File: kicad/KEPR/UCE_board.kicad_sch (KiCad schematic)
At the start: 10 parts, among them U2 STM32G484CETx

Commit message: Mais ajustes no roteamento
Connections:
- net +3.3V: now also U2.9 (PA1)
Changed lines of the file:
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@@
+	(wire
+		(pts
+			(xy 231.14 116.84) (xy 236.22 116.84)
+		)
+		(stroke
+			(width 0)
+			(type default)
+		)
+	)
 	(wire
 		(pts

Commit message: Ajustes no Power Rail, entre outros ajustes.
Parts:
- R2: value GMR320HJAAFD5L00 -> GMR320HJAAFM5L00
- R3: value GMR320HJAAFD5L00 -> GMR320HJAAFS5L00
- R4: value GMR320HJAAFD5L00 -> GMR320HJAAFE5L00
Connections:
- net +3.3V: no longer U2.9 (PA1)
- net I2C_SDA_MCU_CTL: now reaches U2.37 (PA13)
- net I2C_SCL_MCU_CTL: now reaches U2.38 (PA14)
- new net +3.3v Shunt Out: U2.9 (PA1)

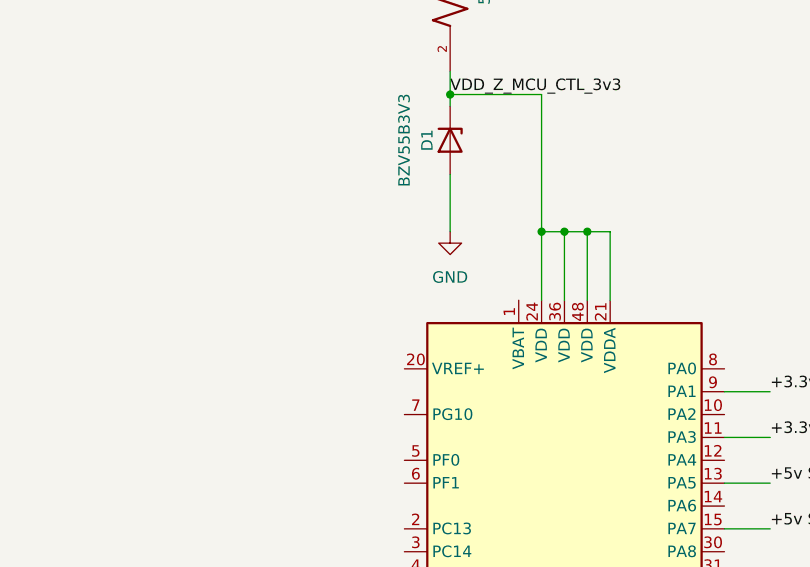
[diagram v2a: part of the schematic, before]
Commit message: Adicionado holder para bateria.
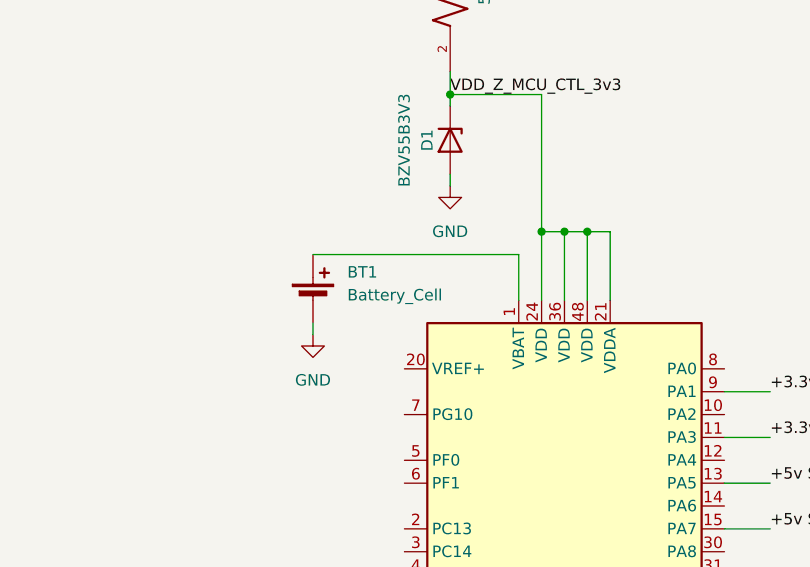
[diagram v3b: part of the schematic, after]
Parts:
- added BT1: Battery_Cell, Battery:BatteryHolder_Multicomp_BC-2001_1x2032, symbol Device:Battery_Cell
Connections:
- net GND: now also BT1.2 (-)
- net at U2.1 (VBAT): now also BT1.1 (+)
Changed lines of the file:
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@@
 	(wire
 		(pts
-			(xy 200.66 92.71) (xy 200.66 99.06)
+			(xy 200.66 92.71) (xy 200.66 93.98)
 		)
 		(stroke
@@
 	(wire
 		(pts
+			(xy 208.28 101.6) (xy 208.28 106.68)
+		)
+		(stroke
+			(width 0)
+			(type default)
+		)
+	)
+	(wire
+		(pts
 			(xy 147.32 236.22) (xy 147.32 246.38)
 		)
@@
 		(pts
 			(xy 200.66 83.82) (xy 200.66 85.09)
+		)
+		(stroke
+			(width 0)
+			(type default)
+		)
+	)
+	(wire
+		(pts
+			(xy 185.42 101.6) (xy 208.28 101.6)
+		)
+		(stroke
+			(width 0)
+			(type default)
+		)
+	)
+	(wire
+		(pts
+			(xy 185.42 109.22) (xy 185.42 110.49)
 		)
 		(stroke
@@
 	(symbol
 		(lib_id "power:GND")
+		(at 185.42 110.49 0)
+		(unit 1)
+		(exclude_from_sim no)
+		(in_bom yes)
+		(on_board yes)
+		(dnp no)
+		(fields_autoplaced yes)
+		(property "Reference" "#PWR02"
+			(at 185.42 116.84 0)
+			(effects
+				(font
+					(size 1.27 1.27)
+				)
+				(hide yes)
+			)
+		)
+		(property "Value" "GND"
+			(at 185.42 115.57 0)
+			(effects
+				(font
+					(size 1.27 1.27)
+				)
+			)
+		)
+		(property "Footprint" ""
+			(at 185.42 110.49 0)
+			(effects
+				(font
+					(size 1.27 1.27)
+				)
+				(hide yes)
+			)
+		)
+		(property "Datasheet" ""
+			(at 185.42 110.49 0)
+			(effects
+				(font
+					(size 1.27 1.27)
+				)
+				(hide yes)
+			)
+		)
+		(property "Description" "Power symbol creates a global label with name \"GND\" , ground"
+			(at 185.42 110.49 0)
+			(effects
+				(font
+					(size 1.27 1.27)
+				)
+				(hide yes)
+			)
+		)
+		(pin "1"
+		)
+		(instances
+			(project "KEPR"
+				(path "/5d9e1dfb-5ec5-4e06-bbdb-9cbfa1c0b9f1/fdc41c7f-76d0-4a6a-9947-620e5325b70e"
+					(reference "#PWR02")
+					(unit 1)
+				)
+			)
+		)
+	)
+	(symbol
+		(lib_id "Device:Battery_Cell")
+		(at 185.42 106.68 0)
+		(unit 1)
+		(exclude_from_sim no)
+		(in_bom yes)
+		(on_board yes)
+		(dnp no)
+		(fields_autoplaced yes)
+		(property "Reference" "BT1"
+			(at 189.23 103.5684 0)
+			(effects
+				(font
+					(size 1.27 1.27)
+				)
+				(justify left)
+			)
+		)
+		(property "Value" "Battery_Cell"
+			(at 189.23 106.1084 0)
+			(effects
+				(font
+					(size 1.27 1.27)
+				)
+				(justify left)
+			)
+		)
+		(property "Footprint" "Battery:BatteryHolder_Multicomp_BC-2001_1x2032"
+			(at 185.42 105.156 90)
+			(effects
+				(font
+					(size 1.27 1.27)
+				)
+				(hide yes)
+			)
+		)
+		(property "Datasheet" "~"
+			(at 185.42 105.156 90)
+			(effects
+				(font
+					(size 1.27 1.27)
+				)
+				(hide yes)
+			)
+		)
+		(property "Description" "Single-cell battery"
+			(at 185.42 106.68 0)
+			(effects
+				(font
+					(size 1.27 1.27)
+				)
+				(hide yes)
+			)
+		)
+		(pin "1"
+		)
+		(pin "2"
+		)
+		(instances
+			(project ""
+				(path "/5d9e1dfb-5ec5-4e06-bbdb-9cbfa1c0b9f1/fdc41c7f-76d0-4a6a-9947-620e5325b70e"
+					(reference "BT1")
+					(unit 1)
+				)
+			)
+		)
+	)
+	(symbol
+		(lib_id "power:GND")
 		(at 147.32 259.08 0)
 		(unit 1)
@@
 	(symbol
 		(lib_id "power:GND")
-		(at 200.66 99.06 0)
+		(at 200.66 93.98 0)
 		(unit 1)
 		(exclude_from_sim no)
@@
 		(fields_autoplaced yes)
 		(property "Reference" "#PWR034"
-			(at 200.66 105.41 0)
+			(at 200.66 100.33 0)
 			(effects
 				(font
@@
 		)
 		(property "Value" "GND"
-			(at 200.66 104.14 0)
+			(at 200.66 99.06 0)
 			(effects
 				(font
@@
 		)
 		(property "Footprint" ""
-			(at 200.66 99.06 0)
+			(at 200.66 93.98 0)
 			(effects
 				(font
@@
 		)
 		(property "Datasheet" ""
-			(at 200.66 99.06 0)
+			(at 200.66 93.98 0)
 			(effects
 				(font
@@
 		)
 		(property "Description" "Power symbol creates a global label with name \"GND\" , ground"
-			(at 200.66 99.06 0)
-			(effects
-				(font
+			(at 200.66 93.98 0)
+			(effects
+				(font

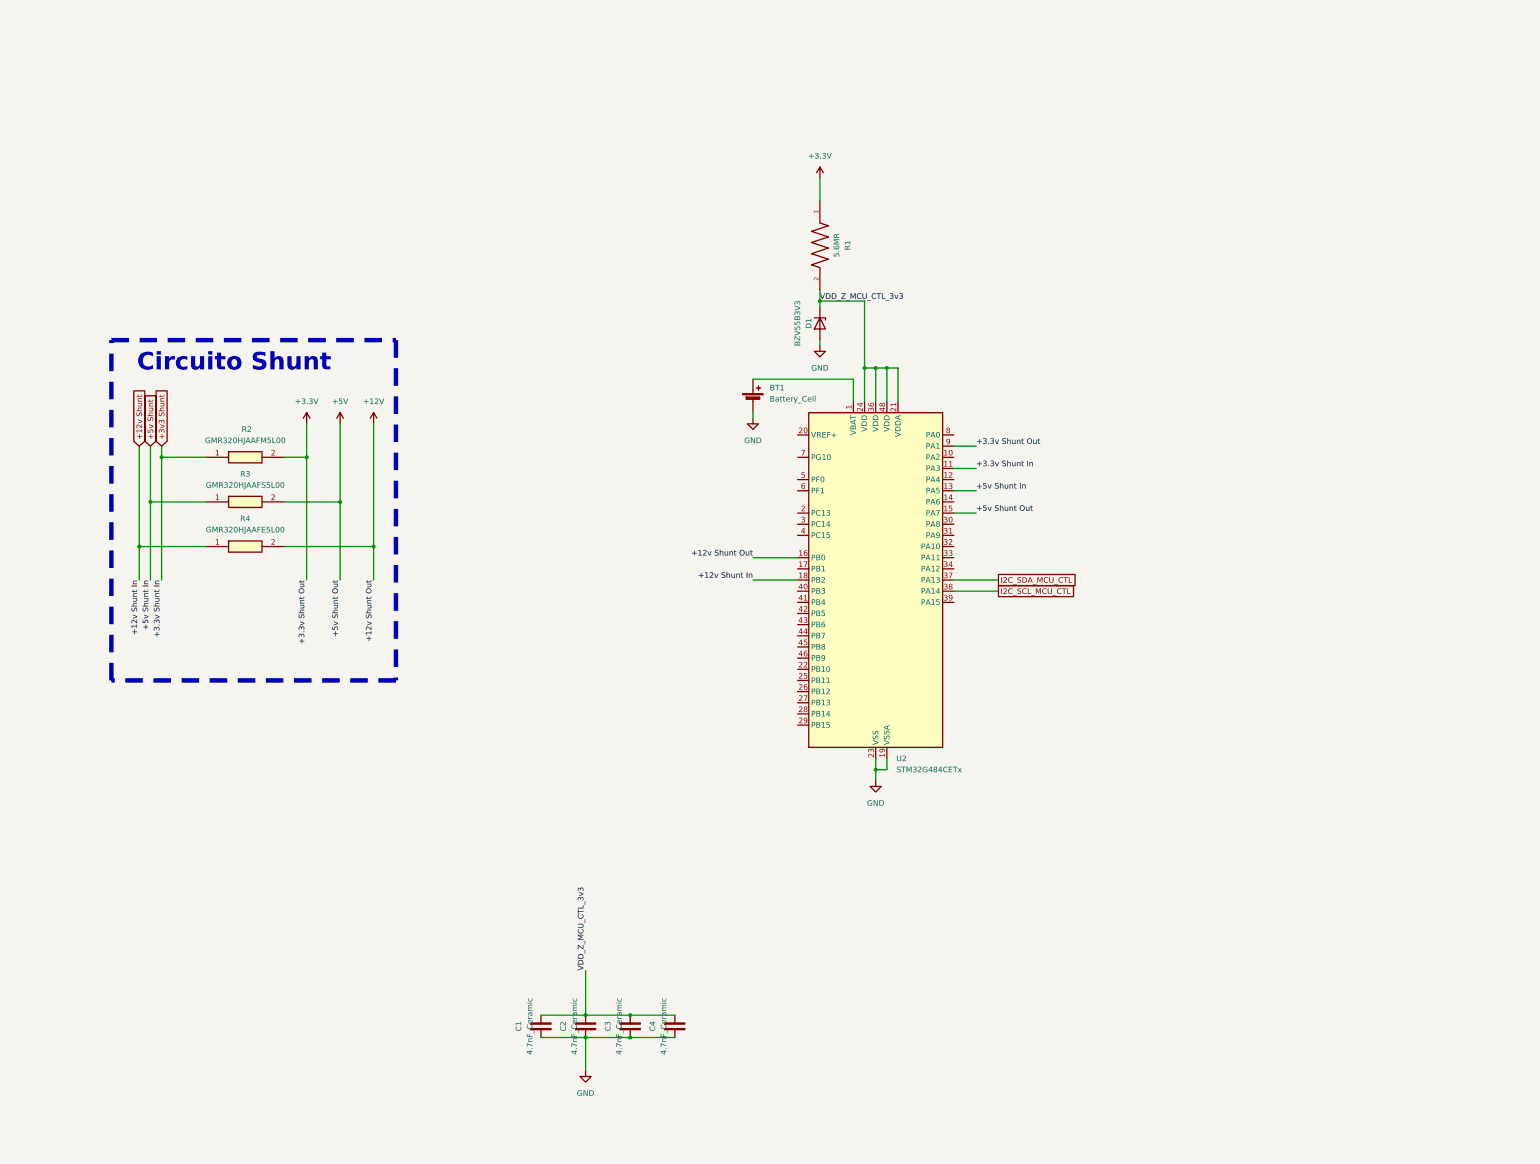
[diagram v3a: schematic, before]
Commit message: Troca dos sensores de corrente e conversores de tensão para o MCU controlador
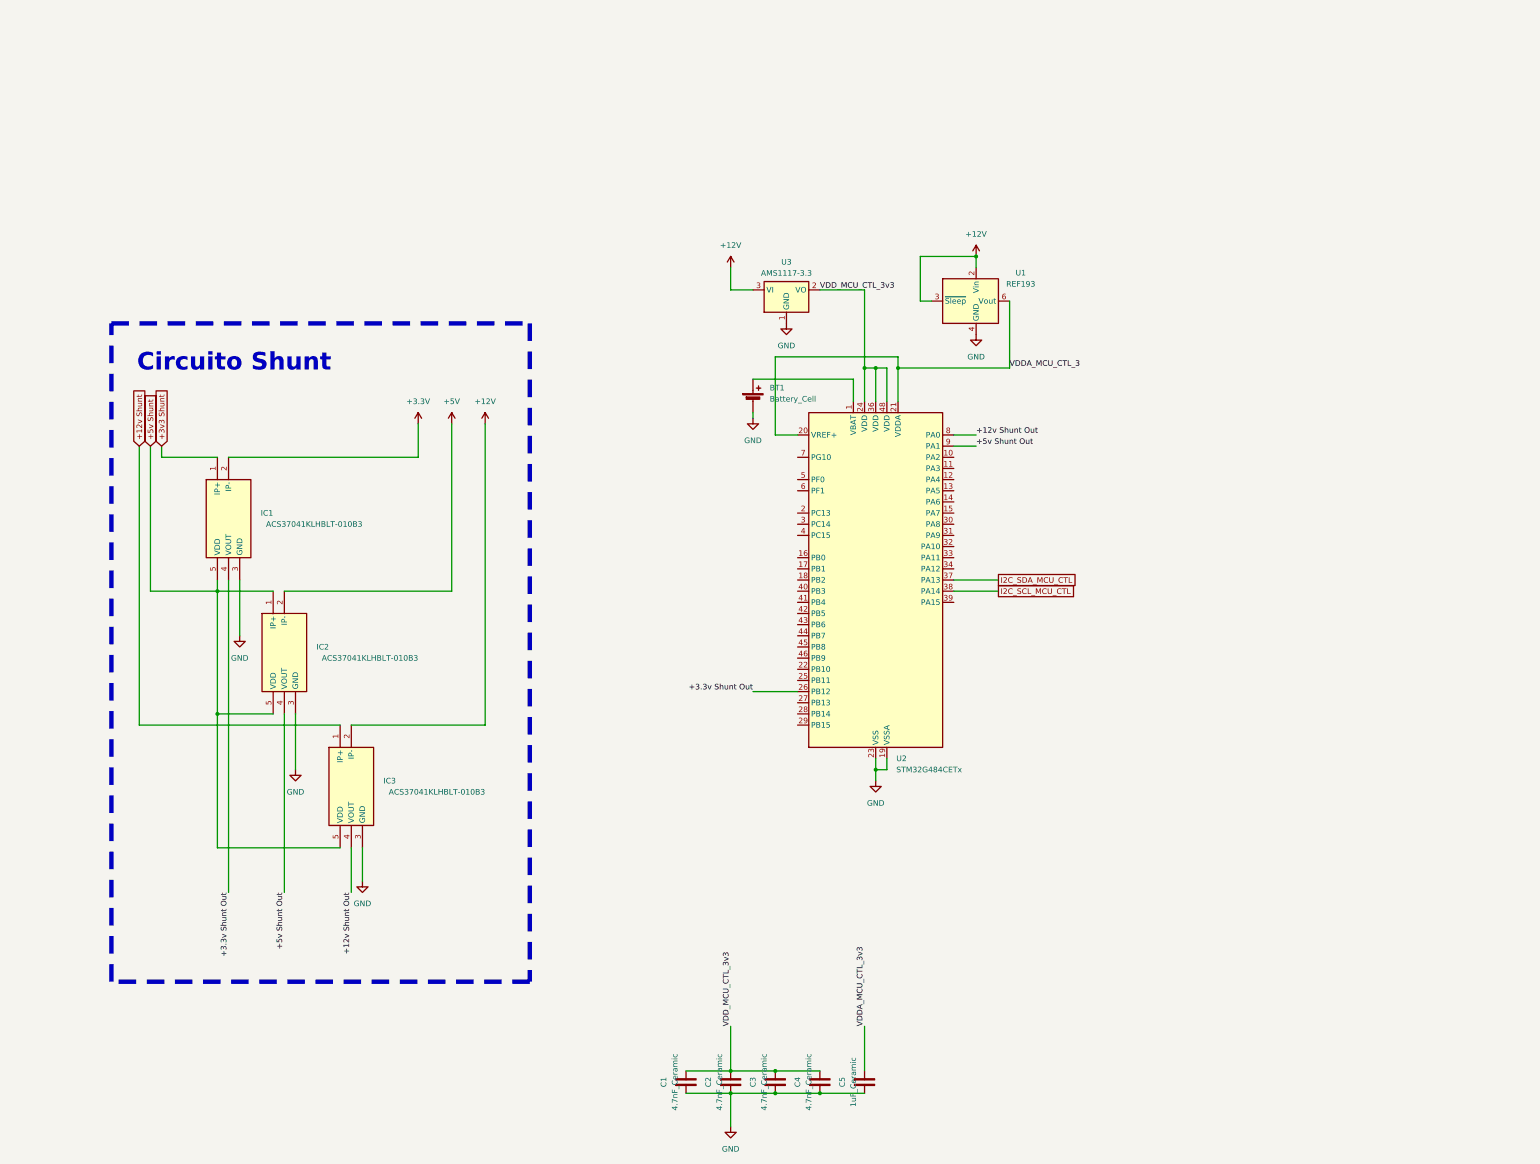
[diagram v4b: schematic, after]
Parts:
- removed D1: BZV55B3V3, Diode_SMD:D_MiniMELF, symbol Diode:BZV55B3V3
- removed R1: 5.6MR, Resistors SMD:RESC2012X60N, symbol CRCW0805100RFKEAC:CRCW0805100RFKEAC
- removed R2: GMR320HJAAFM5L00, Shunt Rohm:RESC7142X55N, symbol Shunt Rohm:GMR320HJAAFD5L00
- removed R3: GMR320HJAAFS5L00, Shunt Rohm:RESC7142X55N, symbol Shunt Rohm:GMR320HJAAFD5L00
- removed R4: GMR320HJAAFE5L00, Shunt Rohm:RESC7142X55N, symbol Shunt Rohm:GMR320HJAAFD5L00
- added C5: 1uF_Ceramic, Capacitor:C_0805_2012Metric, symbol PCM_SL_Capacitors:4.7nF_Ceramic
- added IC1, IC2, IC3: ACS37041KLHBLT-010B3, APS12628LLHALTBAP, symbol ACS37041KLHBLT-010B3:ACS37041KLHBLT-010B3
- added U1: REF193, REF193:SOIC127P600X175-8N, symbol Reference_Voltage:REF193
- added U3: AMS1117-3.3, Package_TO_SOT_SMD:SOT-223-3_TabPin2, symbol Regulator_Linear:AMS1117-3.3
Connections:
- net +12V: now also IC3.2 (IP-), U1.2 (Vin), U1.3 (~{Sleep}), U3.3 (VI); no longer U2.16 (PB0)
- net +12v Shunt: now also IC3.1 (IP+); no longer U2.18 (PB2)
- net +3.3V: now also IC1.2 (IP-)
- net +3.3v Shunt Out: now also U2.26 (PB12), IC1.4 (VOUT); no longer U2.9 (PA1)
- net +3v3 Shunt: now also IC1.1 (IP+); no longer U2.11 (PA3)
- net +5V: now also IC2.2 (IP-); no longer U2.15 (PA7)
- net +5v Shunt: now also IC1.5 (VDD), IC2.1 (IP+), IC2.5 (VDD), IC3.5 (VDD); no longer U2.13 (PA5)
- net GND: now also C5.1, IC1.3 (GND), IC2.3 (GND), IC3.3 (GND), U1.4 (GND), U3.1 (GND)
- net VDDA_MCU_CTL_3: now reaches U2.20 (VREF+)
- net VDDA_MCU_CTL_3: now also U2.21 (VDDA), U1.6 (Vout)
- net +12v Shunt Out: now reaches U2.8 (PA0)
- net +12v Shunt Out: now also IC3.4 (VOUT)
- net VDD_Z_MCU_CTL_3v3 renamed VDD_MCU_CTL_3v3
- net VDD_MCU_CTL_3v3: now also U3.2 (VO); no longer U2.21 (VDDA)
- new net +5v Shunt Out: IC2.4 (VOUT), U2.9 (PA1)
- new net VDDA_MCU_CTL_3v3: C5.2
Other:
- moved on the sheet: C1, C2, C3, C4

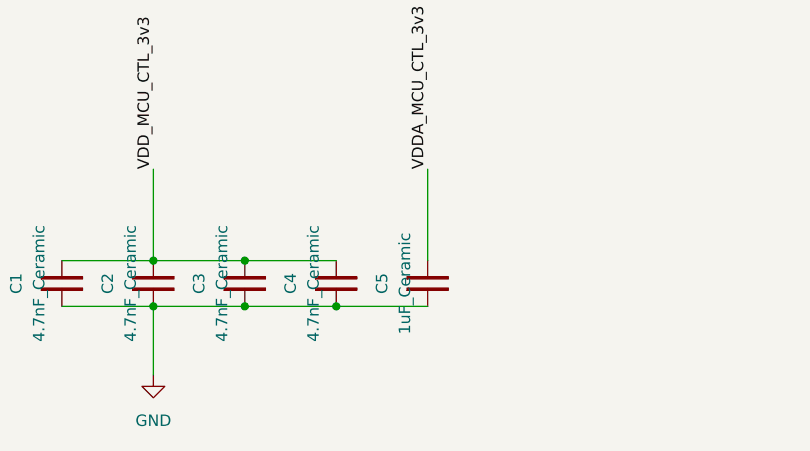
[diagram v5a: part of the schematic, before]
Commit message: Iniciado a distribuição das vias.
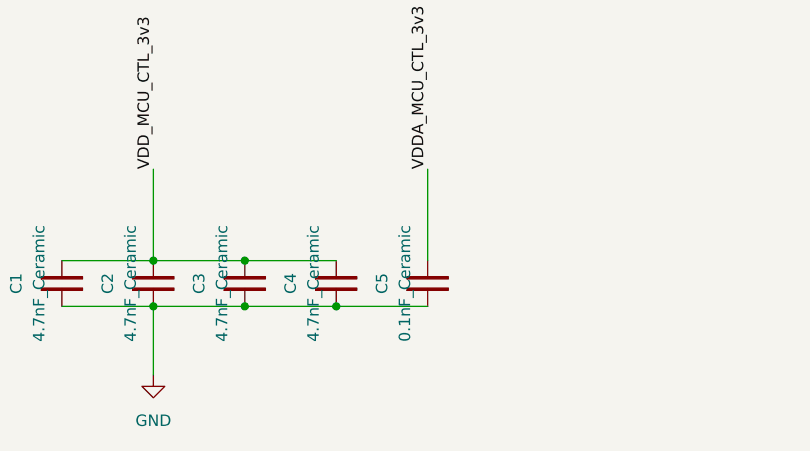
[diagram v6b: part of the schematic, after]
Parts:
- C5: value 1uF_Ceramic -> 0.1nF_Ceramic
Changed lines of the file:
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@@
 			)
 		)
-		(property "Value" "1uF_Ceramic"
+		(property "Value" "0.1nF_Ceramic"
 			(at 208.28 261.62 0)
 			(effects
@@
 			)
 		)
-		(property "Description" "4.7nF Ceramic Capacitor"
+		(property "Description" "0.1nF Ceramic Capacitor"
 			(at 210.82 261.62 0)
 			(effects
